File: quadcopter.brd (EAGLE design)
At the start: 138 x 138 mm, 74 parts, among them J1 ISP, J3 JUMPER, Q1 2.6A, Q2 2.6A, Q3 2.6A, Q4 2.6A, Q5 2.6A, Q7 2.6A, U2 ATMEGA128RFA1, Y1 16MHz

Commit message: Moved silkscreen for legibility. Added labels and orientation reference.
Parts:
- moved U$4 0.30 mm to (-46.2, -0.50)
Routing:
- net N$10: track 88.1 -> 89.5 mm
- net 3V: track 132.7 -> 133.8 mm, vias 12 -> 9
- net PWM_BR: track 89.2 -> 88.2 mm
- net TX0: track 55.1 -> 55.7 mm
- net N$3: track 14.8 -> 14.7 mm, vias 2 -> 0
- net PWM_TR: vias 3 -> 5
- net N$4: vias 2 -> 0
- net N$6: vias 2 -> 4
- added copper zone on layer 1, net FGND
- added copper zone on layer 16, net FGND
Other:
- board text added: "3V"
- board text added: "BGND"
- board text added: "BL"
- board text added: "BR"
- board text added: "DTR"
- board text added: "GND"
- board text added: "PBL"
- board text added: "PBR"
- board text added: "PTL"
- board text added: "PTR"
- board text added: "RXI"
- board text added: "RXO"
- board text added: "SCL"
- board text added: "SDA"
- board text added: "TL"
- board text added: "TR"
- board text added: "TXO"
- board text added: "VBAT"

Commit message: Corrected mistakes found on schematics and libraries. Rerouted board from updated schematic.
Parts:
- removed R14, R16: 10K, quadparts_prebuilt:RESC2012X60_HS
- C12, C14, C17, C8: value 1uF -> 0.1uF
- R12, R13: value 330 -> 10K
- moved R10 70.8 mm to (35.3, 0.40)
- moved R2 50.1 mm to (-0.20, 35.7), turned to 270 degrees
- moved R4 49.6 mm to (-35.6, 1.00), turned to 0 degrees
- moved C12 0.61 mm to (-0.10, 31.1)
- moved R8 0.45 mm to (0.70, -35.9)
- moved C8 0.41 mm to (30.6, 0.40)
- moved C14 0.10 mm to (0.60, -31.0)
- turned D5 to 30 degrees
- turned D6 to 180 degrees
- turned D7 to 20 degrees
- turned D8 to 202.5 degrees
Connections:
- net BAT_GND: now also C4.2, U$6.2; no longer R14.1, R16.1
- net FILTERED_BL: now also C17.2, R4.2; no longer R10.2
- net FILTERED_BR: now also C14.2
- net FILTERED_TL: now also C12.2, R2.2; no longer R4.2
- net FILTERED_TR: now also C8.2, R10.2; no longer R2.2
- net GND: no longer C4.2, U$6.2
- net LED_B: no longer R14.2
- net LED_R: no longer R16.2
- net PWM_BL: now also R4.1; no longer C17.2, R10.1
- net PWM_BR: no longer C14.2
- net PWM_TL: now also R2.1; no longer C12.2, R4.1
- net PWM_TR: now also R10.1; no longer C8.2, R2.1
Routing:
- net FGND: track 0.00 -> 50.7 mm
- net 3V: track 133.8 -> 90.5 mm
- net PWM_BR: track 88.2 -> 112.8 mm
- net N$10: track 89.5 -> 112.6 mm
- net GND: track 123.9 -> 106.1 mm, vias 30 -> 39
- net RESET: track 93.0 -> 108.2 mm, vias 3 -> 2
- net BAT_GND: track 217.0 -> 230.2 mm, vias 1 -> 3
- net SCL: track 54.4 -> 67.0 mm, vias 2 -> 1
- net V_BAT: track 105.4 -> 94.5 mm, vias 8 -> 9
- net LED_R: track 52.3 -> 44.0 mm
- net PWM_BL: track 68.5 -> 76.7 mm
- net N$6: track 81.1 -> 74.2 mm, vias 4 -> 2
- net PWM_TR: track 75.4 -> 80.9 mm, vias 5 -> 3
- net PB6: track 26.2 -> 31.3 mm
- net N$4: track 13.7 -> 18.1 mm
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- removed copper zone on layer 1, net N$14
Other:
- board text added: "CSE 190 Quad v0 Brian Henriquez Jason Lam"

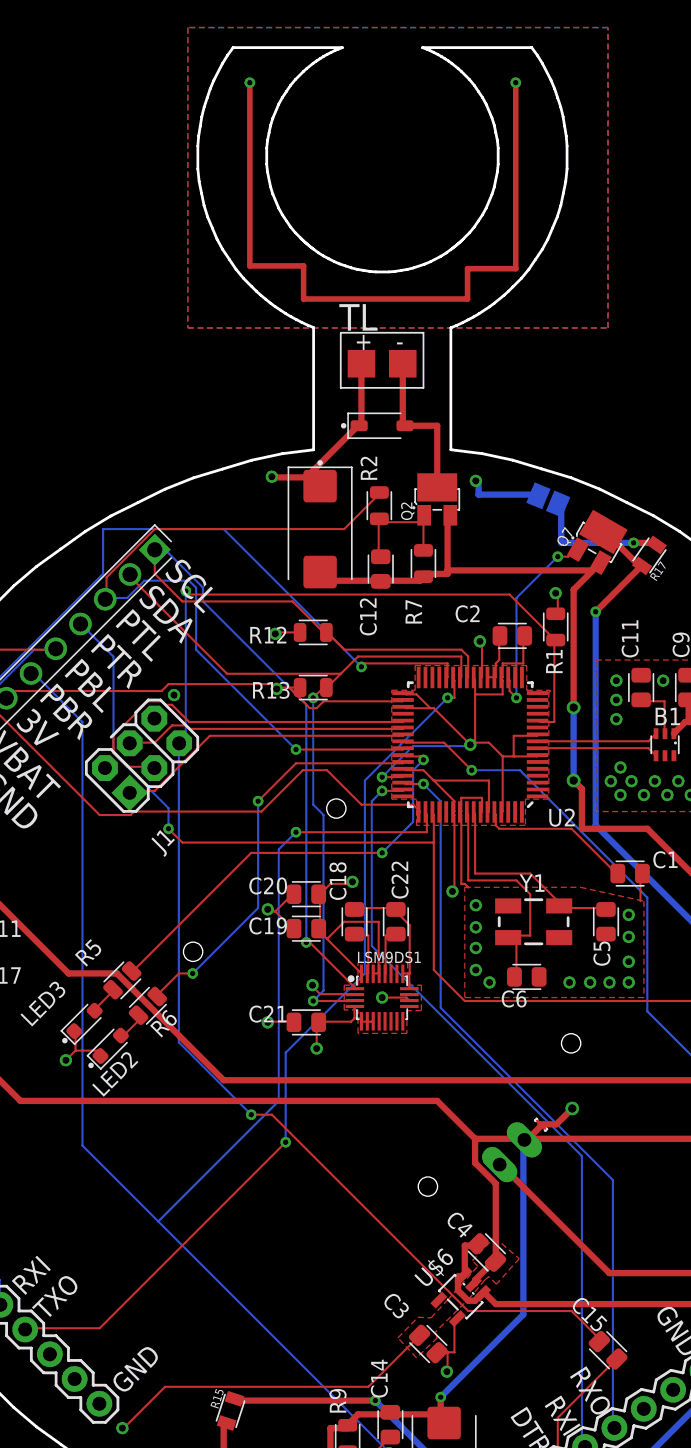
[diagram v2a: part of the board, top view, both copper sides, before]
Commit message: Added a logo to the board. Updated libary with logo.
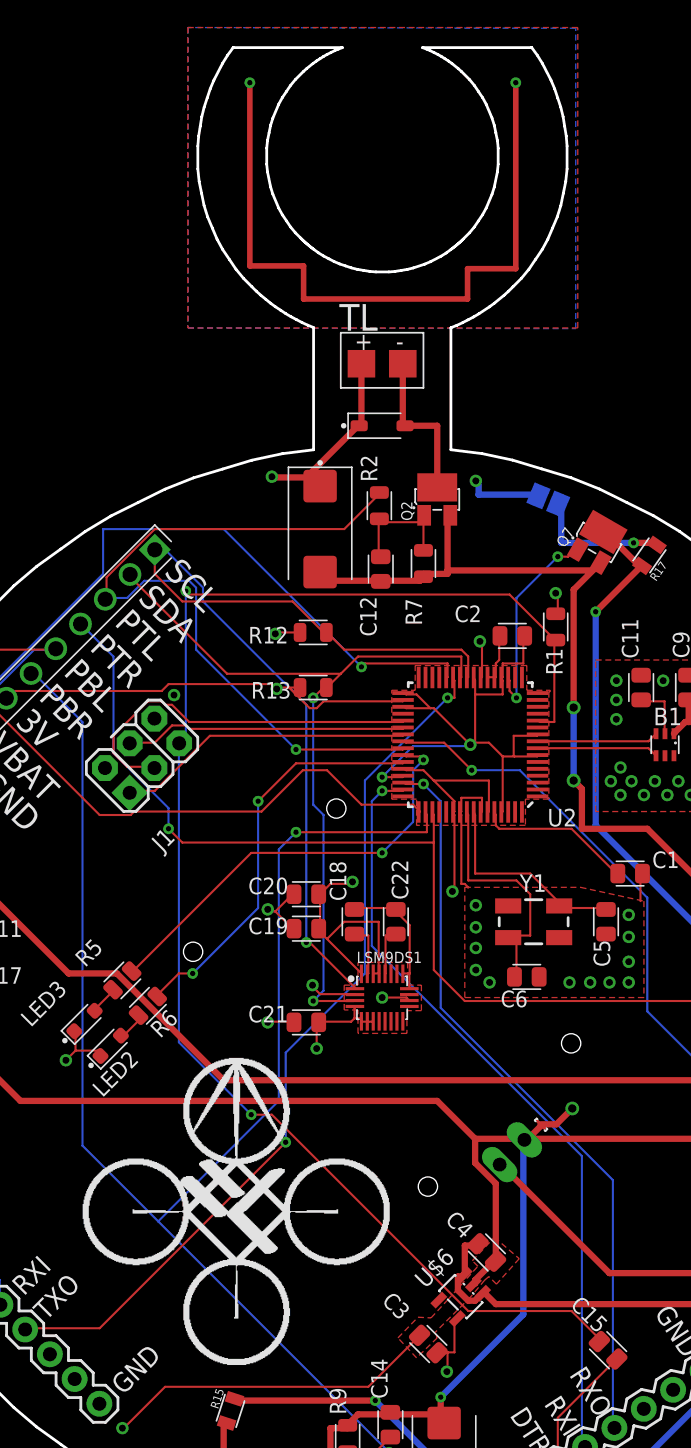
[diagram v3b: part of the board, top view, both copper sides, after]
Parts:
- added U$7: (no value), quadparts:LOGO_QUAD
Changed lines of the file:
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@@
 <attribute name="VALUE" x="36.85" y="-0.9" size="1.2" layer="27" font="vector" ratio="10"/>
 </element>
+<element name="U$7" library="quadparts" package="LOGO_QUAD" value="" x="-21.7" y="-26.7"/>
 </elements>
 <signals>
@@
 <vertex x="-14.1" y="70.4"/>
 <vertex x="-14.1" y="48.6"/>
-<vertex x="16.4" y="48.6"/>
-<vertex x="16.4" y="70.4"/>
+<vertex x="14.2" y="48.6"/>
+<vertex x="14.2" y="70.4"/>
 </polygon>
 <via x="-9.6" y="66.4" extent="1-16" drill="0.381"/>
@@
 <vertex x="-14.1" y="70.4"/>
 <vertex x="-14.1" y="48.6"/>
-<vertex x="16.4" y="48.6"/>
-<vertex x="16.4" y="70.4"/>
+<vertex x="14.05" y="48.55"/>
+<vertex x="14.05" y="70.35"/>
 </polygon>
 <wire x1="-9.6" y1="66.4" x2="-9.6" y2="53.1" width="0.4064" layer="1"/>

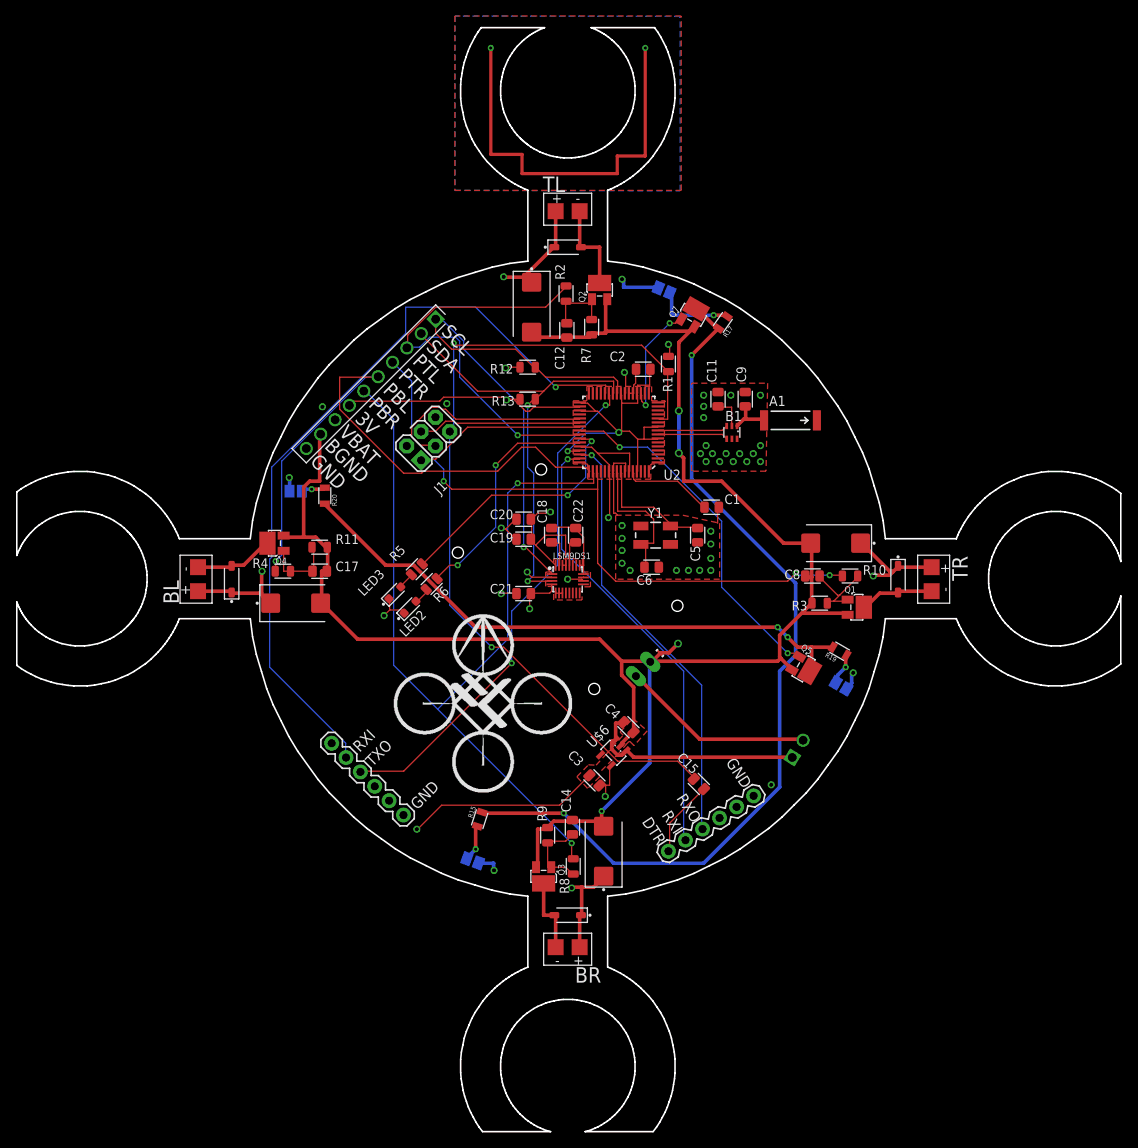
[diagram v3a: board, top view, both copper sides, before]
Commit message: Finished new routing & added cam zip
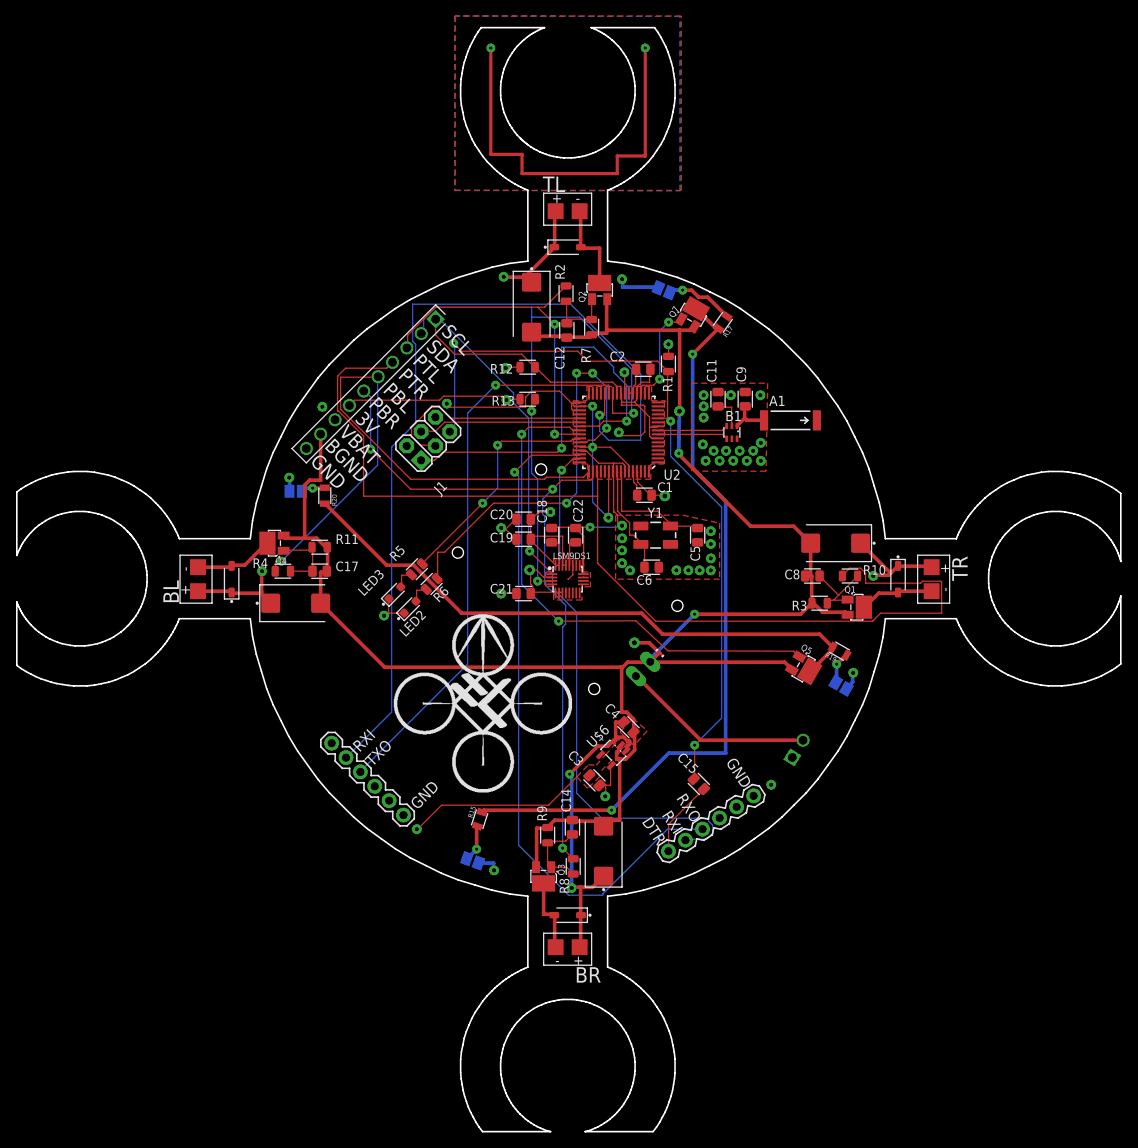
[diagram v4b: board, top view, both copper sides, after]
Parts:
- moved C1 8.53 mm to (9.60, 10.5)
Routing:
- net PWM_TR: track 80.9 -> 129.6 mm, vias 3 -> 0
- net RX0: track 54.0 -> 85.0 mm
- net MISO: track 21.7 -> 51.9 mm, vias 0 -> 2
- net PWM_BR: track 112.8 -> 87.5 mm, vias 2 -> 3
- net PB7: track 29.5 -> 52.5 mm, vias 2 -> 4
- net SDA: track 57.6 -> 80.3 mm, vias 2 -> 3
- net LED_R: track 44.0 -> 64.9 mm
- net N$10: track 112.6 -> 93.5 mm
- net GND: track 106.1 -> 125.2 mm, vias 39 -> 38
- net TX1: track 97.6 -> 111.8 mm
- net TX0: track 56.0 -> 68.7 mm
- net RESET: track 108.2 -> 96.1 mm, vias 2 -> 3
- net PWM_TL: track 54.0 -> 43.9 mm, vias 1 -> 2
- net AVDD: track 11.3 -> 3.25 mm
- net RX1: track 63.6 -> 70.5 mm, vias 2 -> 1
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- added copper zone on layer 2, net N$1

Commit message: Updated board and cam to meet new board review changes.
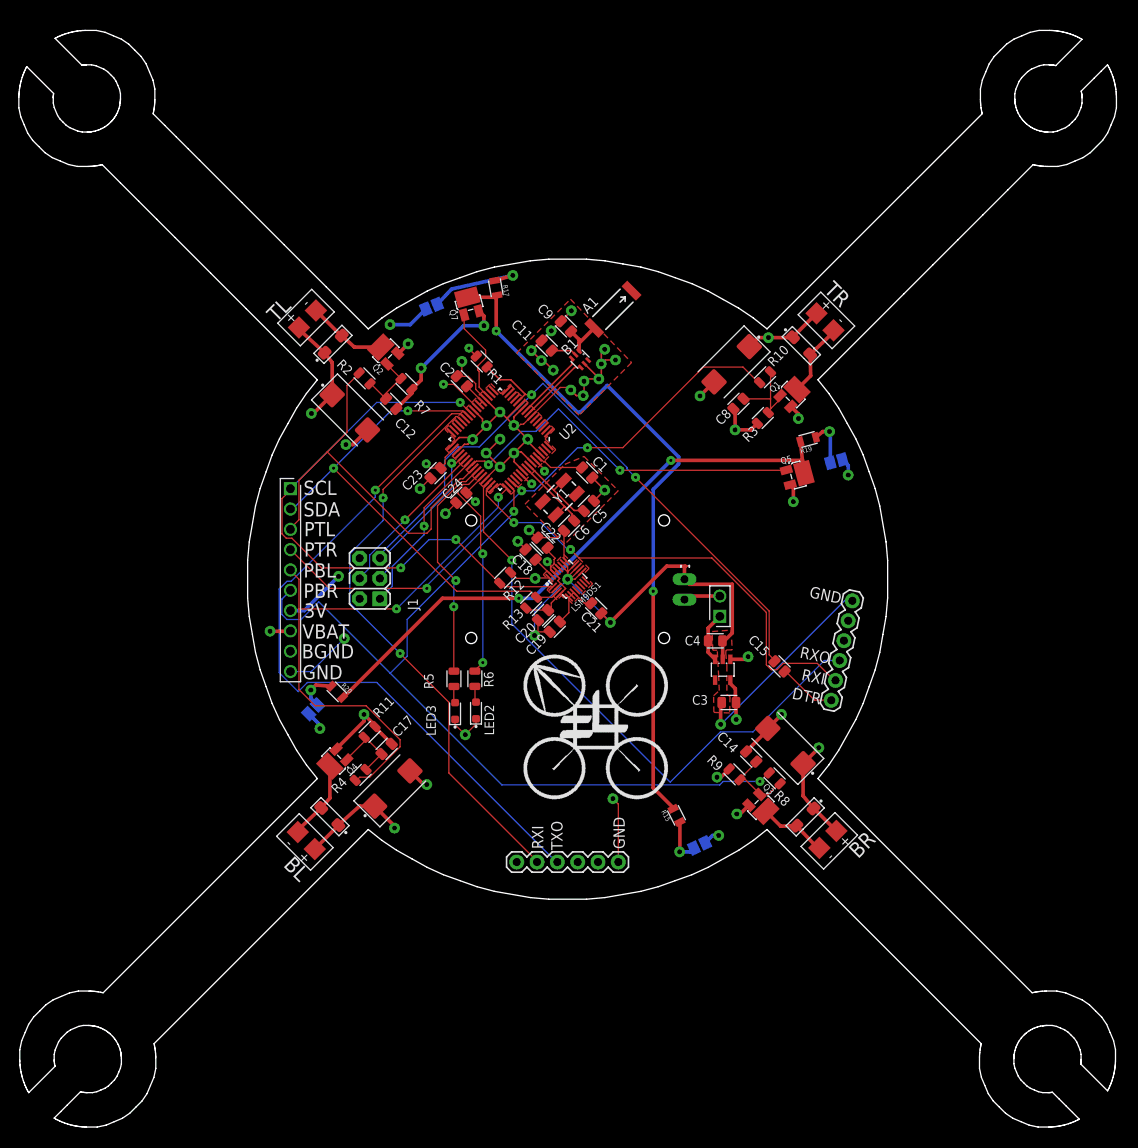
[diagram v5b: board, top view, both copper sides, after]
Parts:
- added C23, C24: 1uF, quadparts_prebuilt:CAPC2012X140_HS
- moved U$4 35.4 mm to (-32.3, -33.0), turned to 135 degrees
- moved U$2 35.2 mm to (-32.9, 32.2), turned to 45 degrees
- moved U$3 35.2 mm to (32.9, -32.2), turned to 225 degrees
- moved U$1 34.8 mm to (31.8, 32.5), turned to 315 degrees
- moved D3 32.1 mm to (29.7, -29.7), turned to 225 degrees
- moved D4 32.1 mm to (-29.7, -29.7), turned to 135 degrees
- moved D2 31.8 mm to (-29.3, 29.3), turned to 45 degrees
- moved D1 31.6 mm to (29.2, 29.2), turned to 315 degrees
- moved D8 29.1 mm to (-17.0, 34.1), turned to 157.5 degrees
- moved R17 28.7 mm to (-8.98, 36.4), turned to 100 degrees
- moved D7 28.4 mm to (16.5, -33.3), turned to 335 degrees
- moved D5 28.1 mm to (33.6, 14.8), turned to 345 degrees
- moved J2 27.9 mm to (-34.6, 11.3), turned to 270 degrees
- moved JP1 27.8 mm to (33.0, -15.1), turned to 78 degrees
- moved Q3 27.6 mm to (23.3, -27.6), turned to 225 degrees
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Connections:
- net 3V: now also C23.1, C24.1
- net GND: now also C23.2, C24.2
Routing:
- net BAT_GND: track 233.5 -> 78.4 mm, vias 3 -> 13
- net GND: track 125.2 -> 200.2 mm, vias 38 -> 34
- net PWM_TR: track 129.6 -> 74.8 mm, vias 0 -> 3
- net FGND: track 50.7 -> 0.00 mm, vias 2 -> 0
- net TX1: track 111.8 -> 72.0 mm, vias 1 -> 2
- net 3V: track 94.4 -> 59.2 mm
- net MISO: track 51.9 -> 21.6 mm, vias 2 -> 1
- net PB7: track 52.5 -> 27.9 mm, vias 4 -> 2
- net V_BAT: track 93.9 -> 73.4 mm
- net N$2: track 24.2 -> 4.60 mm
- net LED_R: track 64.9 -> 45.9 mm
- net RX1: track 70.5 -> 89.1 mm
- net PWM_BR: track 87.5 -> 105.8 mm, vias 3 -> 2
- net SDA: track 80.3 -> 62.6 mm, vias 3 -> 2
- net RX0: track 85.0 -> 74.9 mm
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- added copper zone on layer 15, net BAT_GND
- removed copper zone on layer 1, net FGND
- removed copper zone on layer 16, net FGND
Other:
- board size 138 x 138 mm -> 137.2 x 137.1 mm

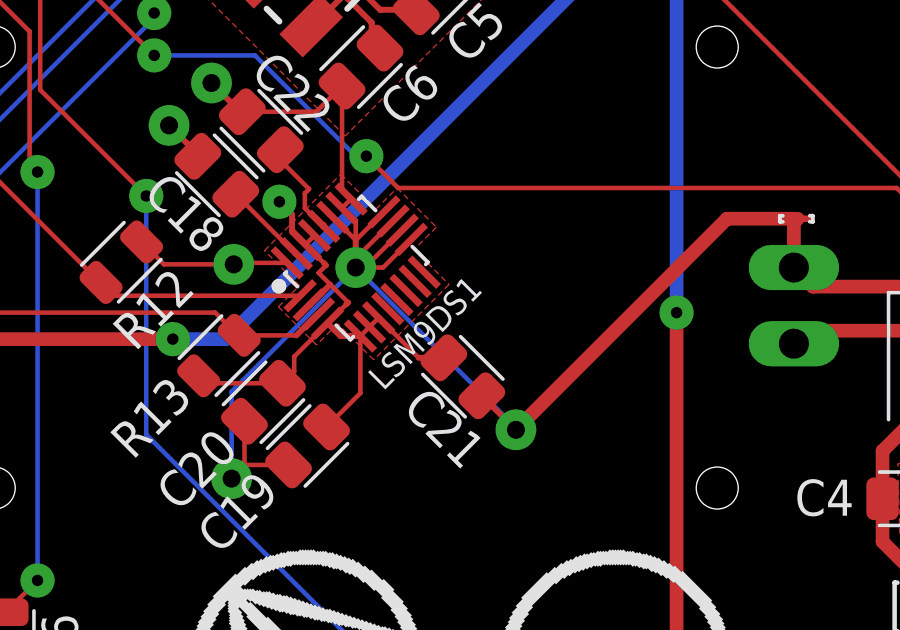
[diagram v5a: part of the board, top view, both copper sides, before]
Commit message: Completed board routing
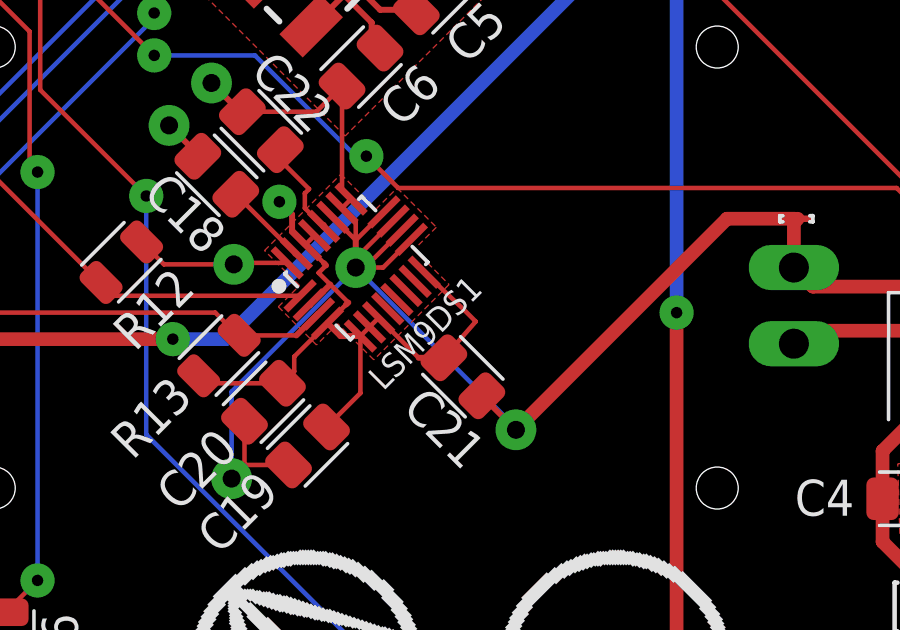
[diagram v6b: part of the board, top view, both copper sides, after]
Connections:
- net 3V: now also LSM9DS1.13
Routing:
- net 3V: track 59.2 -> 63.1 mm
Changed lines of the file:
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@@
 <wire x1="-12.6607375" y1="10.815196875" x2="-12.653675" y2="10.815196875" width="0.1524" layer="1"/>
 <wire x1="-12.653675" y1="10.815196875" x2="-11.5258375" y2="9.6873625" width="0.1524" layer="1"/>
+<contactref element="LSM9DS1" pad="13"/>
+<wire x1="2.283953125" y1="-0.1555625" x2="3.6" y2="-1.4" width="0.1524" layer="1"/>
+<wire x1="3.6" y1="-1.4" x2="4" y2="-1.8" width="0.1524" layer="1"/>
+<wire x1="4" y1="-1.8" x2="2.938021875" y2="-3.008728125" width="0.1524" layer="1"/>
 </signal>
 <signal name="FLYBACK_BR" class="2">
